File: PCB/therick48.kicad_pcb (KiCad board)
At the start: 2 copper layers, 226.5 x 75.8 mm, 124 parts, among them J1 TYPE-C-31-M12_13, J2 AVR-ISP-6, K1 KEYSW, K10 KEYSW, K11 KEYSW, K12 KEYSW, K13 KEYSW, K14 KEYSW, K15 KEYSW, K16 KEYSW, K17 KEYSW, K18 KEYSW, K19 KEYSW, K2 KEYSW, K20 KEYSW, K21 KEYSW, K22 KEYSW, K23 KEYSW, K24 KEYSW, K25 KEYSW, K26 KEYSW, K27 KEYSW, K28 KEYSW, K29 KEYSW, K3 KEYSW, K30 KEYSW, K31 KEYSW, K32 KEYSW, K33 KEYSW, K34 KEYSW, K35 KEYSW, K36 KEYSW, K37 KEYSW, K38 KEYSW, K39 KEYSW, K4 KEYSW, K40 KEYSW, K41 KEYSW, K42 KEYSW, K43 KEYSW, K44 KEYSW, K45 KEYSW, K46 KEYSW, K47 KEYSW, K48 KEYSW, K5 KEYSW, K6 KEYSW, K7 KEYSW, K8 KEYSW, K9 KEYSW, SW1 SW_PUSH, U1 ATMEGA32U4, U2 HOLE, U3 USBLC6-2SC6, Y1 16MHz

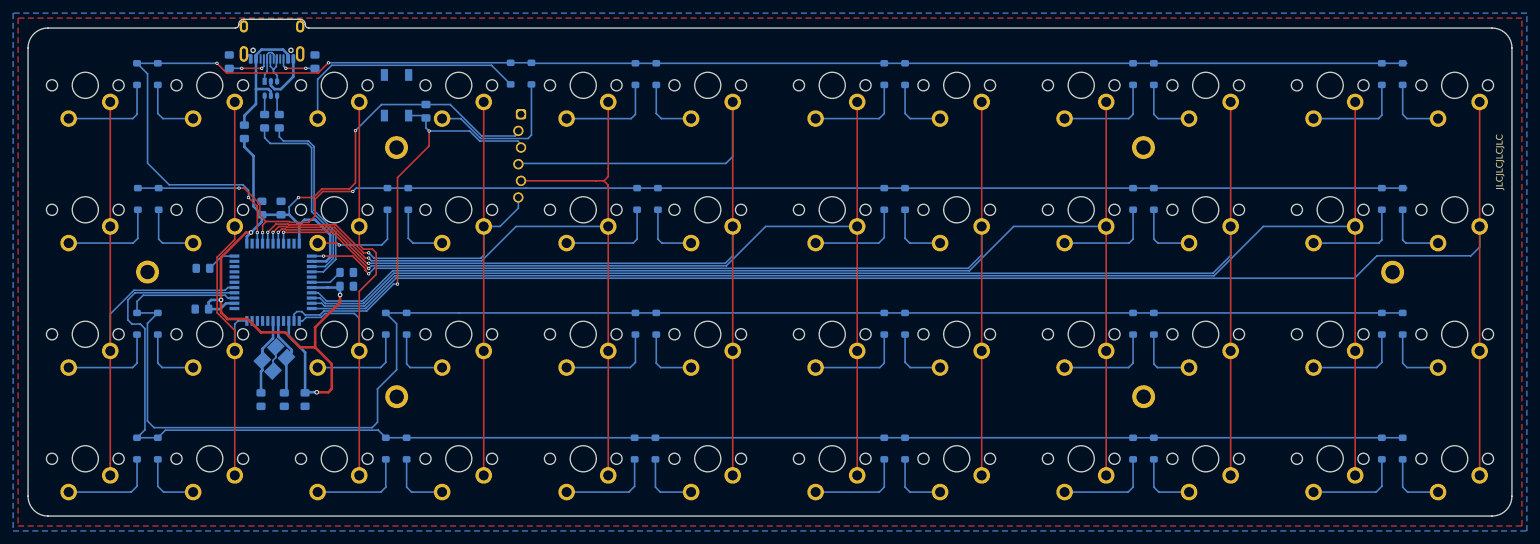
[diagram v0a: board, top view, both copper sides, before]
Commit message: Updated mounting holes
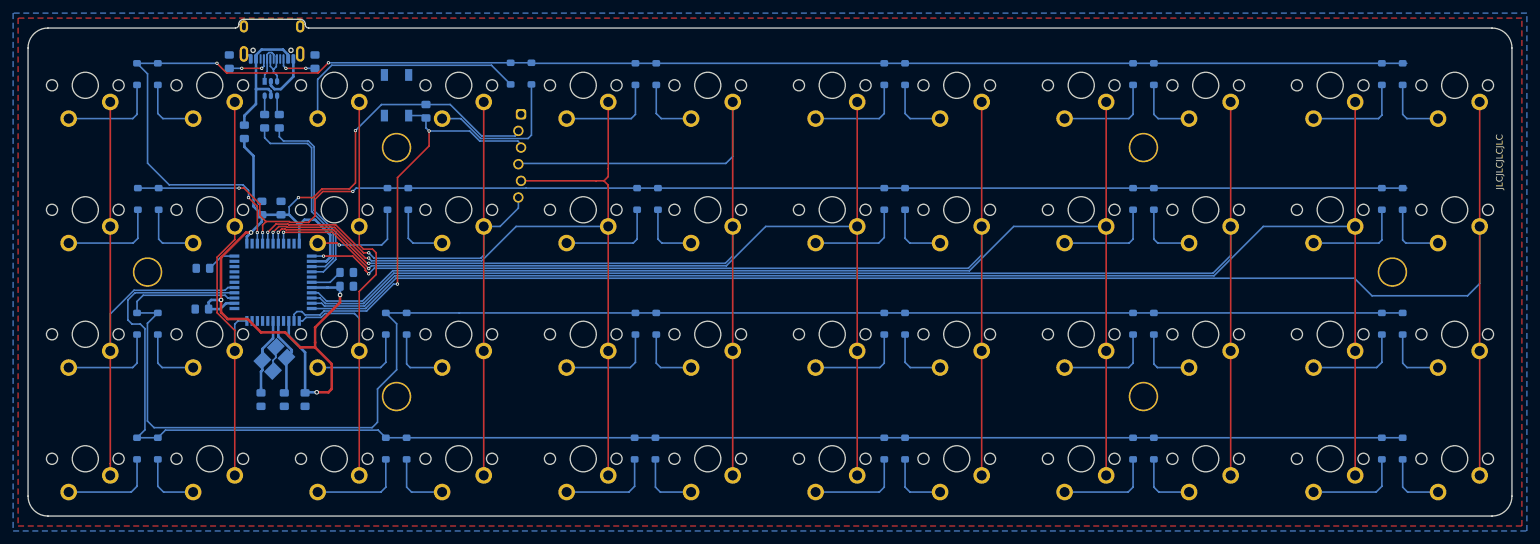
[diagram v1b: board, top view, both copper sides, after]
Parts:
- H1, H2, H3, H4, H5, H6: footprint random-keyboard-parts:Generic-Mounthole -> random-keyboard-parts:plate_hole_4mm_tht
- moved H1 2.03 mm to (64.9, 75.0)
- moved H2 2.03 mm to (102.9, 56.0)
- moved H4 2.03 mm to (216.9, 56.0)
- moved H3 2.01 mm to (102.9, 94.0)
- moved H5 2.01 mm to (216.9, 94.0)
- moved H6 2.01 mm to (254.9, 75.0)
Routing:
- net col11: track 242.3 -> 247.8 mm
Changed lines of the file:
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@@
     (uvia_drill 0.2)
   )
+  (module random-keyboard-parts:plate_hole_4mm_tht locked (layer F.Cu)
+    (at 254.9292 74.992)
+    (fp_text reference H6 (at 0.381 1.4097) (layer Dwgs.User)
+      (effects (font (size 1 1) (thickness 0.15)))
+    )
+    (fp_text value MountingHole (at 0 -0.5) (layer F.Fab)
+      (effects (font (size 1 1) (thickness 0.15)))
+    )
+    (pad 1 thru_hole circle (at 0.0508 -2.032) (size 4.5 4.5) (drill 4) (layers *.Cu *.Mask))
+  )
+  (module random-keyboard-parts:plate_hole_4mm_tht locked (layer F.Cu)
+    (at 216.9292 93.992)
+    (fp_text reference H5 (at 0.381 1.4097) (layer Dwgs.User)
+      (effects (font (size 1 1) (thickness 0.15)))
+    )
+    (fp_text value MountingHole (at 0 -0.5) (layer F.Fab)
+      (effects (font (size 1 1) (thickness 0.15)))
+    )
+    (pad 1 thru_hole circle (at 0.0508 -2.032) (size 4.5 4.5) (drill 4) (layers *.Cu *.Mask))
+  )
+  (module random-keyboard-parts:plate_hole_4mm_tht locked (layer F.Cu)
+    (at 216.9292 55.992)
+    (fp_text reference H4 (at 0.381 1.4097) (layer Dwgs.User)
+      (effects (font (size 1 1) (thickness 0.15)))
+    )
+    (fp_text value MountingHole (at 0 -0.5) (layer F.Fab)
+      (effects (font (size 1 1) (thickness 0.15)))
+    )
+    (pad 1 thru_hole circle (at 0.0508 -2.032) (size 4.5 4.5) (drill 4) (layers *.Cu *.Mask))
+  )
+  (module random-keyboard-parts:plate_hole_4mm_tht locked (layer F.Cu)
+    (at 102.9292 93.992)
+    (fp_text reference H3 (at 0.381 1.4097) (layer Dwgs.User)
+      (effects (font (size 1 1) (thickness 0.15)))
+    )
+    (fp_text value MountingHole (at 0 -0.5) (layer F.Fab)
+      (effects (font (size 1 1) (thickness 0.15)))
+    )
+    (pad 1 thru_hole circle (at 0.0508 -2.032) (size 4.5 4.5) (drill 4) (layers *.Cu *.Mask))
+  )
+  (module random-keyboard-parts:plate_hole_4mm_tht (layer F.Cu)
+    (at 102.9292 55.992)
+    (fp_text reference H2 (at 0.381 1.4097) (layer Dwgs.User)
+      (effects (font (size 1 1) (thickness 0.15)))
+    )
+    (fp_text value MountingHole (at 0 -0.5) (layer F.Fab)
+      (effects (font (size 1 1) (thickness 0.15)))
+    )
+    (pad 1 thru_hole circle (at 0.0508 -2.032) (size 4.5 4.5) (drill 4) (layers *.Cu *.Mask))
+  )
+  (module random-keyboard-parts:plate_hole_4mm_tht locked (layer F.Cu)
+    (at 64.9292 74.992)
+    (fp_text reference H1 (at 0.381 1.4097) (layer Dwgs.User)
+      (effects (font (size 1 1) (thickness 0.15)))
+    )
+    (fp_text value MountingHole (at 0 -0.5) (layer F.Fab)
+      (effects (font (size 1 1) (thickness 0.15)))
+    )
+    (pad 1 thru_hole circle (at 0.0508 -2.032) (size 4.5 4.5) (drill 4) (layers *.Cu *.Mask))
+  )
   (module Capacitor_SMD:C_0805_2012Metric_Pad1.15x1.40mm_HandSolder (layer B.Cu)
     (at 95.377 75.13)
@@
     )
   )
-  (module random-keyboard-parts:Generic-Mounthole locked (layer F.Cu)
-    (at 255.005 72.985)
-    (attr virtual)
-    (fp_text reference H6 (at 0 2) (layer Dwgs.User)
-      (effects (font (size 1 1) (thickness 0.15)))
-    )
-    (fp_text value MountingHole (at 0 -2) (layer Dwgs.User)
-      (effects (font (size 1 1) (thickness 0.15)))
-    )
-    (pad 1 thru_hole circle (at 0 0) (size 3.5 3.5) (drill 2.2) (layers *.Cu *.Mask))
-  )
-  (module random-keyboard-parts:Generic-Mounthole locked (layer F.Cu)
-    (at 217.005 91.985)
-    (attr virtual)
-    (fp_text reference H5 (at 0 2) (layer Dwgs.User)
-      (effects (font (size 1 1) (thickness 0.15)))
-    )
-    (fp_text value MountingHole (at 0 -2) (layer Dwgs.User)
-      (effects (font (size 1 1) (thickness 0.15)))
-    )
-    (pad 1 thru_hole circle (at 0 0) (size 3.5 3.5) (drill 2.2) (layers *.Cu *.Mask))
-  )
-  (module random-keyboard-parts:Generic-Mounthole locked (layer F.Cu)
-    (at 216.98 53.96)
-    (attr virtual)
-    (fp_text reference H4 (at 0 2) (layer Dwgs.User)
-      (effects (font (size 1 1) (thickness 0.15)))
-    )
-    (fp_text value MountingHole (at 0 -2) (layer Dwgs.User)
-      (effects (font (size 1 1) (thickness 0.15)))
-    )
-    (pad 1 thru_hole circle (at 0 0) (size 3.5 3.5) (drill 2.2) (layers *.Cu *.Mask))
-  )
-  (module random-keyboard-parts:Generic-Mounthole locked (layer F.Cu)
-    (at 103.005 91.985)
-    (attr virtual)
-    (fp_text reference H3 (at 0 2) (layer Dwgs.User)
-      (effects (font (size 1 1) (thickness 0.15)))
-    )
-    (fp_text value MountingHole (at 0 -2) (layer Dwgs.User)
-      (effects (font (size 1 1) (thickness 0.15)))
-    )
-    (pad 1 thru_hole circle (at 0 0) (size 3.5 3.5) (drill 2.2) (layers *.Cu *.Mask))
-  )
-  (module random-keyboard-parts:Generic-Mounthole (layer F.Cu)
-    (at 102.98 53.96)
-    (attr virtual)
-    (fp_text reference H2 (at 0 2) (layer Dwgs.User)
-      (effects (font (size 1 1) (thickness 0.15)))
-    )
-    (fp_text value MountingHole (at 0 -2) (layer Dwgs.User)
-      (effects (font (size 1 1) (thickness 0.15)))
-    )
-    (pad 1 thru_hole circle (at 0 0) (size 3.5 3.5) (drill 2.2) (layers *.Cu *.Mask))
-  )
-  (module random-keyboard-parts:Generic-Mounthole locked (layer F.Cu)
-    (at 64.98 72.96)
-    (attr virtual)
-    (fp_text reference H1 (at 0 2) (layer Dwgs.User)
-      (effects (font (size 1 1) (thickness 0.15)))
-    )
-    (fp_text value MountingHole (at 0 -2) (layer Dwgs.User)
-      (effects (font (size 1 1) (thickness 0.15)))
-    )
-    (pad 1 thru_hole circle (at 0 0) (size 3.5 3.5) (drill 2.2) (layers *.Cu *.Mask))
-  )
   (module Artwork:rick_large (layer B.Cu)
     (at 237.60625 76.025 180)
@@
   (segment (start 235.273414 66) (end 227.748365 73.525049) (width 0.25) (layer B.Cu) (net 70))
   (segment (start 249.29 66) (end 235.273414 66) (width 0.25) (layer B.Cu) (net 70))
-  (segment (start 90.0375 78.525) (end 98.259 78.525) (width 0.25) (layer B.Cu) (net 71))
   (segment (start 268.29 104) (end 268.29 85) (width 0.25) (layer F.Cu) (net 71))
   (segment (start 268.29 85) (end 268.29 47) (width 0.25) (layer F.Cu) (net 71))
-  (segment (start 98.259 78.525) (end 102.878942 73.905058) (width 0.25) (layer B.Cu) (net 71))
   (segment (start 102.878942 73.905058) (end 249.182942 73.905058) (width 0.25) (layer B.Cu) (net 71))
-  (segment (start 249.182942 73.905058) (end 252.603 70.485) (width 0.25) (layer B.Cu) (net 71))
-  (segment (start 252.603 70.485) (end 266.954 70.485) (width 0.25) (layer B.Cu) (net 71))
-  (segment (start 268.29 69.149) (end 266.954 70.485) (width 0.25) (layer B.Cu) (net 71))
-  (segment (start 268.29 66) (end 268.29 69.149) (width 0.25) (layer B.Cu) (net 71))
+  (segment (start 98.259 78.525) (end 102.878942 73.905058) (width 0.25) (layer B.Cu) (net 71))
+  (segment (start 90.0375 78.525) (end 98.259 78.525) (width 0.25) (layer B.Cu) (net 71))
+  (segment (start 268.29 66) (end 268.29 74.737) (width 0.25) (layer B.Cu) (net 71))
+  (segment (start 268.29 74.737) (end 266.446 76.581) (width 0.25) (layer B.Cu) (net 71))
+  (segment (start 251.858884 76.581) (end 249.182942 73.905058) (width 0.25) (layer B.Cu) (net 71))
+  (segment (start 266.446 76.581) (end 251.858884 76.581) (width 0.25) (layer B.Cu) (net 71))
   (segment (start 76.3275 70.525) (end 74.4625 72.39) (width 0.25) (layer B.Cu) (net 72))
   (segment (start 78.2375 70.525) (end 76.3275 70.525) (width 0.25) (layer B.Cu) (net 72))

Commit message: Added more mounting holes
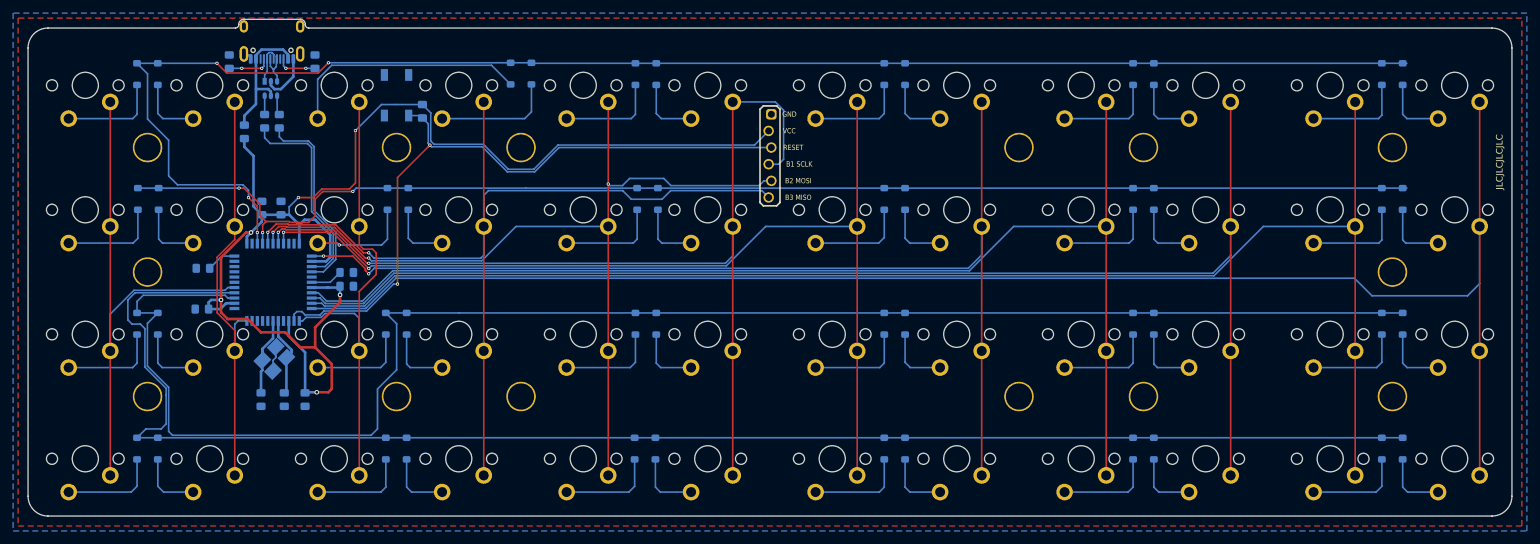
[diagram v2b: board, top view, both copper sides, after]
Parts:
- added H10: MountingHole, random-keyboard-parts:plate_hole_4mm_tht, F.Cu at (121.9, 94.0)
- added H11: MountingHole, random-keyboard-parts:plate_hole_4mm_tht, F.Cu at (254.9, 94.0)
- added H12: MountingHole, random-keyboard-parts:plate_hole_4mm_tht, F.Cu at (197.9, 94.0)
- added H13: MountingHole, random-keyboard-parts:plate_hole_4mm_tht, F.Cu at (121.9, 56.0)
- added H14: MountingHole, random-keyboard-parts:plate_hole_4mm_tht, F.Cu at (197.9, 56.0)
- added H7: MountingHole, random-keyboard-parts:plate_hole_4mm_tht, F.Cu at (64.9, 56.0)
- added H8: MountingHole, random-keyboard-parts:plate_hole_4mm_tht, F.Cu at (254.9, 56.0)
- added H9: MountingHole, random-keyboard-parts:plate_hole_4mm_tht, F.Cu at (64.9, 94.0)
- moved J2 38.2 mm to (160.0, 55.2)
- moved RSW1 0.54 mm to (106.9, 48.4)
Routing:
- net VCC: track 167.7 -> 212.2 mm
- net col3: track 107.0 -> 149.0 mm
- net ISP_Reset: track 64.9 -> 105.1 mm
- net col5: track 176.5 -> 153.8 mm
- net col4: track 127.8 -> 140.8 mm, vias 2 -> 3
- net Net-(D4-Pad2): track 22.6 -> 18.2 mm
- net row3: track 234.2 -> 237.3 mm
- net row0: track 236.4 -> 235.6 mm
- net row2: track 247.2 -> 247.7 mm

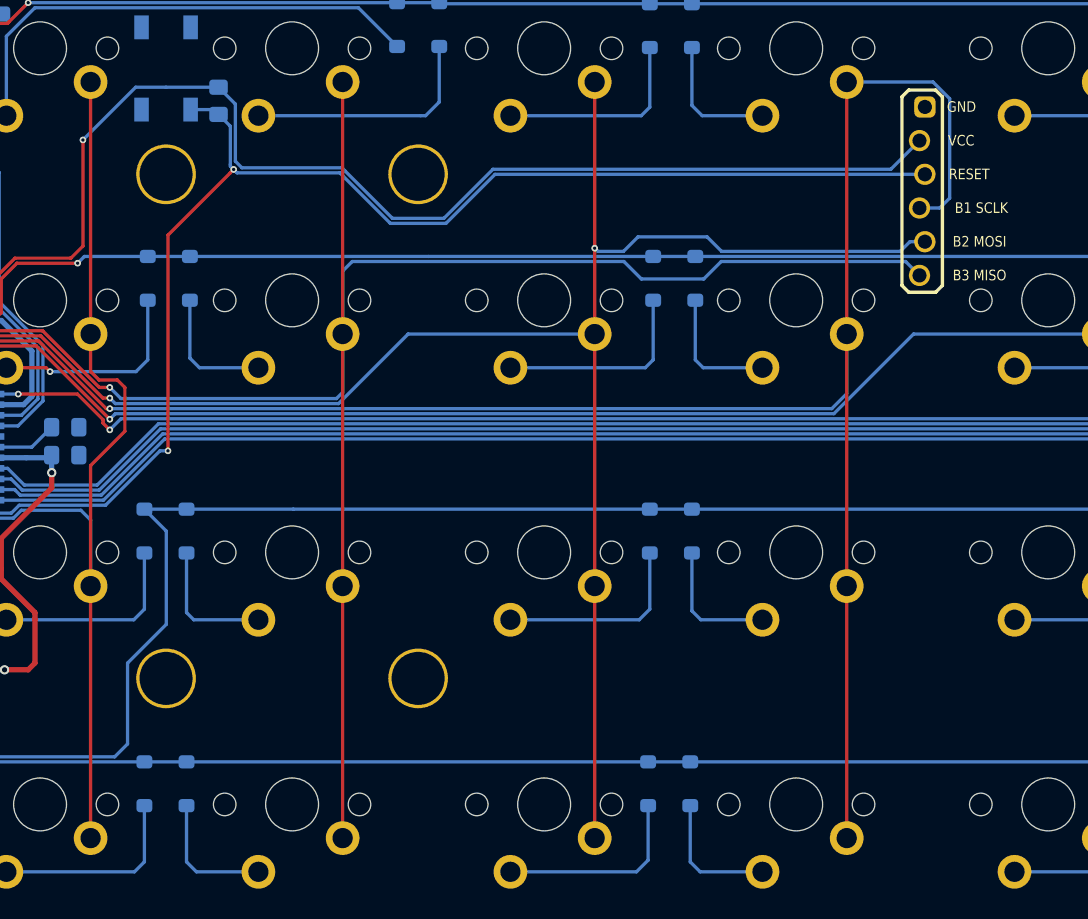
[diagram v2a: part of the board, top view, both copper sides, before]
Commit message: Move ISP Header
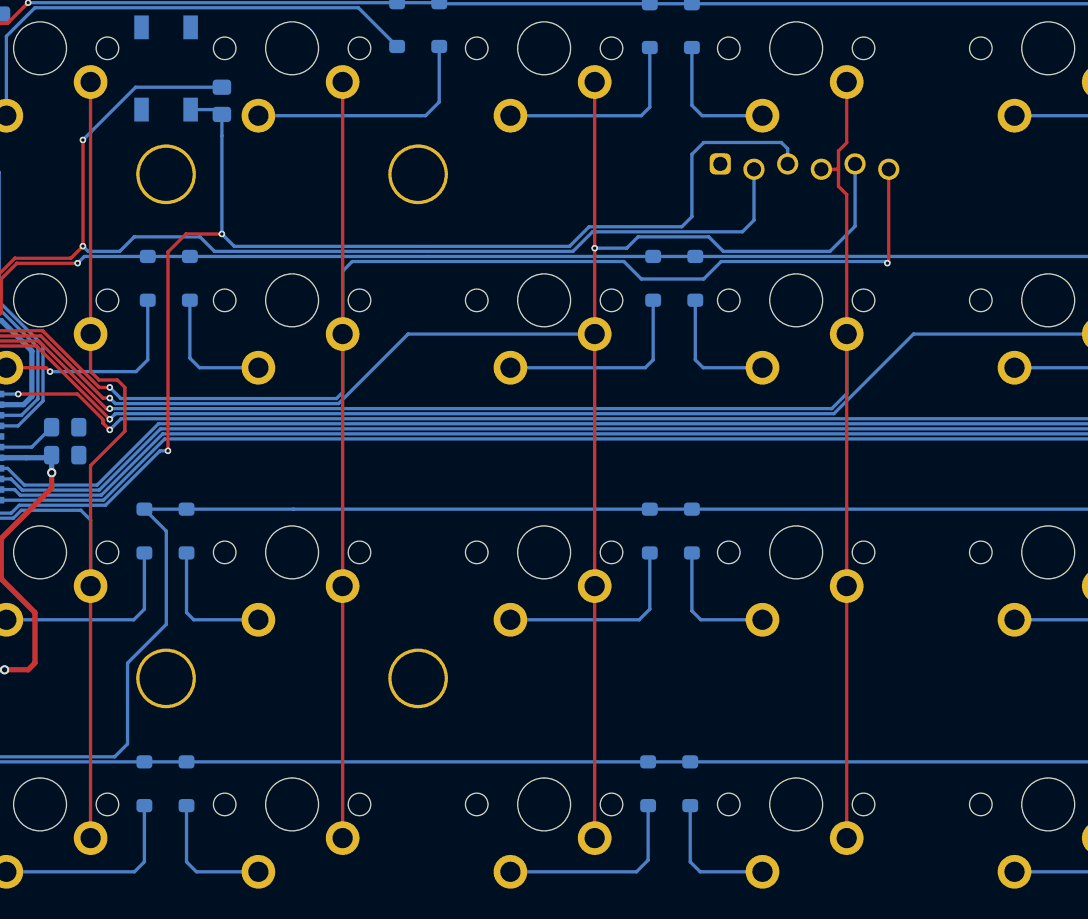
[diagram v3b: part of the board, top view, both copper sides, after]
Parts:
- moved J2 9.06 mm to (151.1, 53.4), turned to 270 degrees
- moved RSW1 0.25 mm to (107.2, 48.4)
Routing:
- net col5: track 153.8 -> 137.2 mm
- net VCC: track 212.2 -> 207.1 mm, vias 6 -> 7
- net col3: track 149.0 -> 153.3 mm, vias 2 -> 3
- net ISP_Reset: track 105.1 -> 101.1 mm

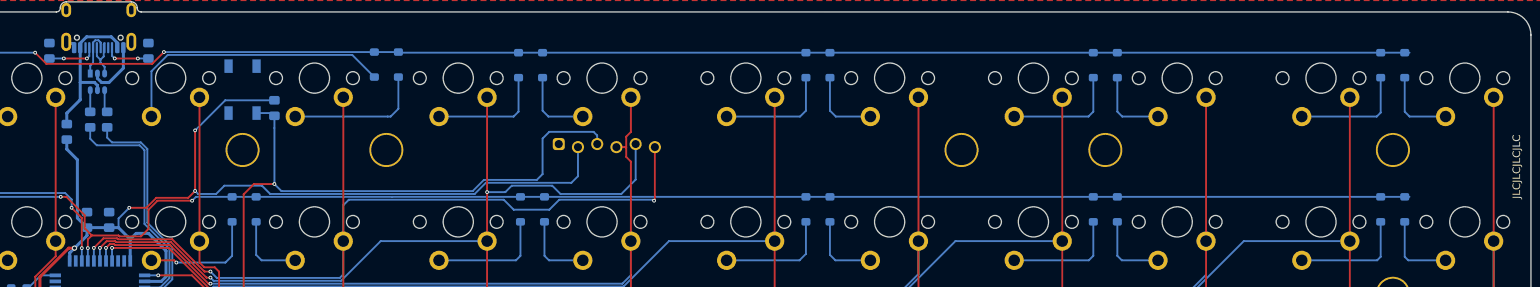
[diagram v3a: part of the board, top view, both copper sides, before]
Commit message: Made ISP header actually work
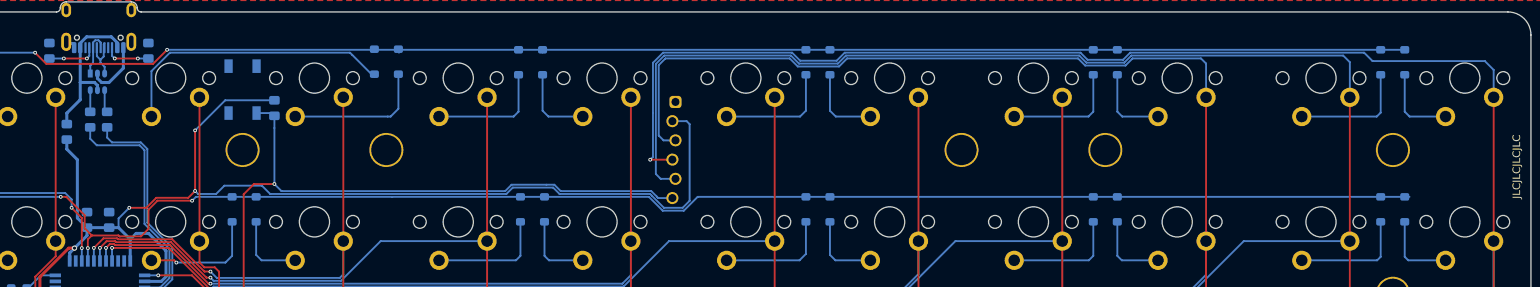
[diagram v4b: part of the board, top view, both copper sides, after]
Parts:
- J2: value AVR-ISP-6 -> AVR-ISP-6_mod
- moved J2 8.89 mm to (160.0, 54.0), turned to 180 degrees
- moved D3 0.38 mm to (120.4, 42.3)
- moved D4 0.38 mm to (123.6, 42.3)
- moved D5 0.38 mm to (139.4, 42.4)
- moved D6 0.38 mm to (142.6, 42.4)
- moved D10 0.38 mm to (218.6, 42.4)
- moved D11 0.38 mm to (253.4, 42.4)
- moved D12 0.38 mm to (256.5, 42.4)
- moved D7 0.38 mm to (177.4, 42.4)
- moved D8 0.38 mm to (180.6, 42.4)
- moved D9 0.38 mm to (215.4, 42.4)
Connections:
- J2 pad 1: col3 -> ISP_Reset
- J2 pad 3: col5 -> col11
- J2 pad 4: col4 -> col10
- J2 pad 5: ISP_Reset -> col9
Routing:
- net col11: track 247.8 -> 381.5 mm, vias 0 -> 1
- net col10: track 221.5 -> 337.7 mm
- net col9: track 205.1 -> 295.9 mm
- net col3: track 153.3 -> 99.0 mm, vias 3 -> 2
- net col4: track 140.5 -> 114.6 mm, vias 3 -> 2
- net VCC: track 207.1 -> 231.4 mm
- net ISP_Reset: track 101.1 -> 104.8 mm
- net col5: track 137.2 -> 135.4 mm
- net row1: track 204.1 -> 205.6 mm
